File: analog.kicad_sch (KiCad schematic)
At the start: 47 parts, among them J10 Sensor harness, U8 ADS1115

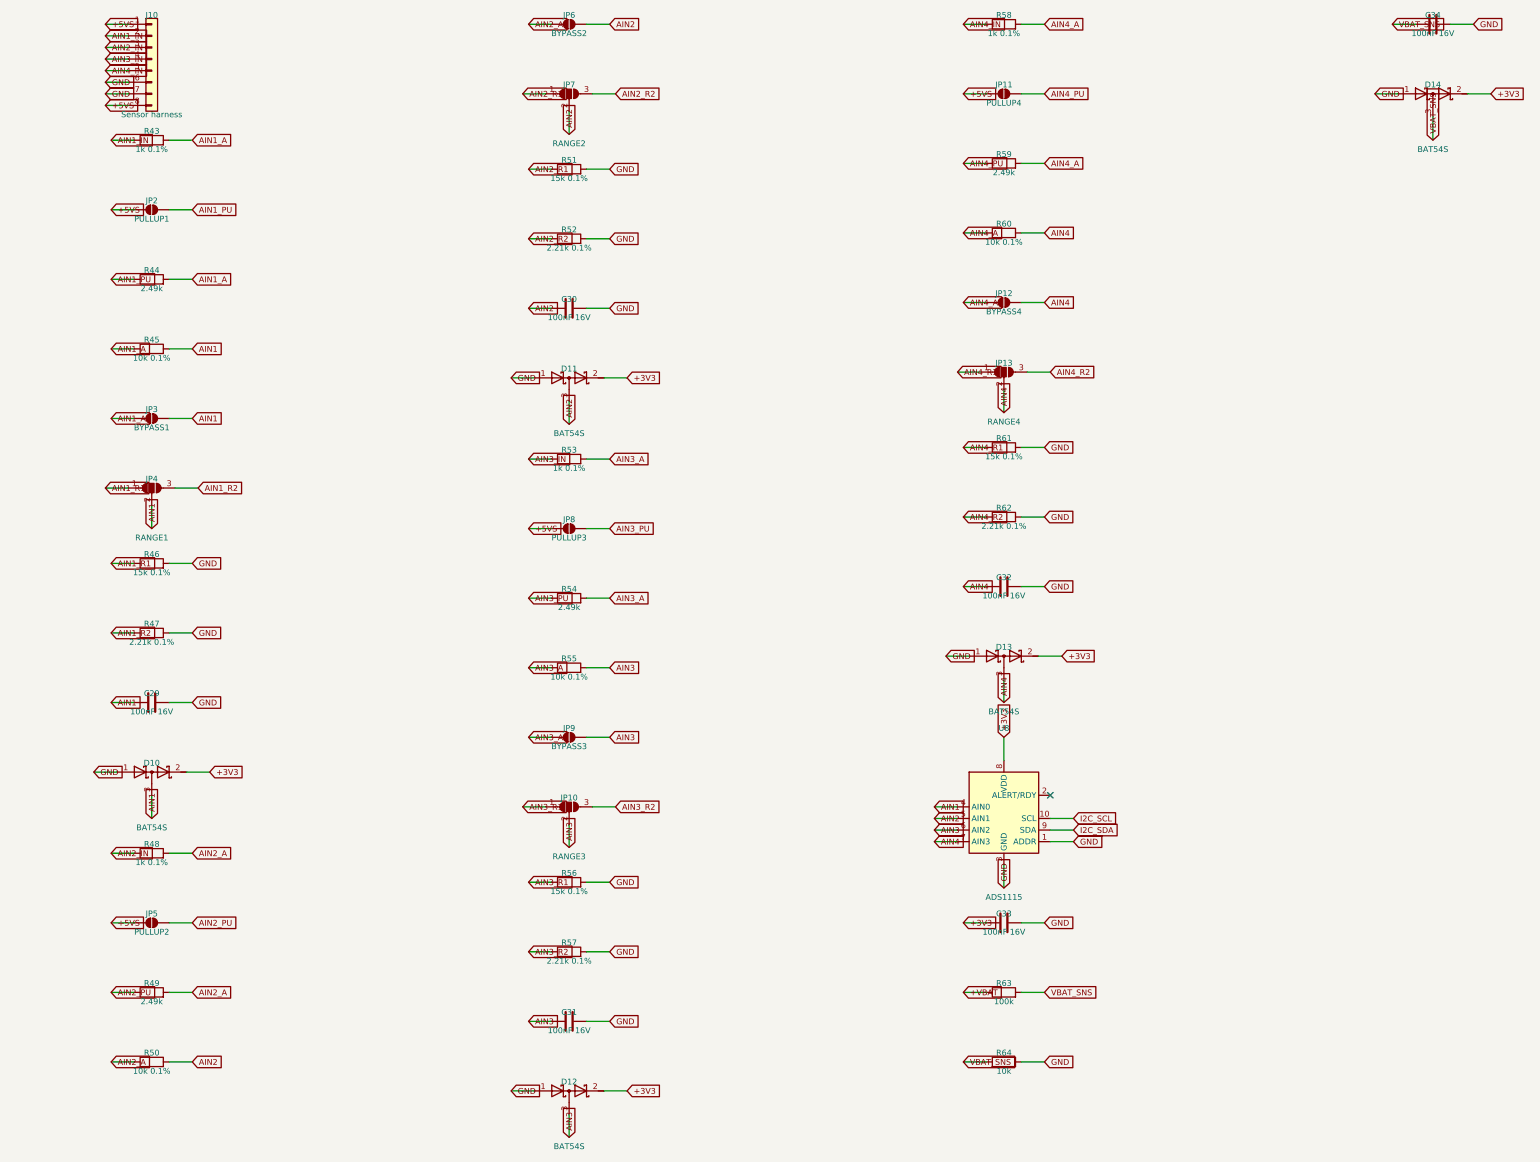
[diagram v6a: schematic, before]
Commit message: Schematic: power symbols and readable text placement (items 1-2 of 5)
The schematic was a netlist drawn as a picture: 486 global labels for 108
nets, roughly four per net, every part an island with a name flag on each
pin and no wires between anything. You could not trace a circuit by eye.
That is a fair description of a document that fails at the one thing a
schematic is for, and it is on me -- the generator was built to produce a
correct netlist and the drawing was an afterthought.

Two of the five agreed fixes are in:

Rails are power symbols. GND, +3V3, +5V, +5VS, +VBAT, VBUS and SD_VDD now
carry a proper power symbol instead of a net-name label -- 190 of them,
taking the label count from 486 to 296. Where KiCad has no stock symbol
for a rail a generic one is instantiated with its Value overridden, which
is how KiCad names a power net; validate.py re-extracts through KiCad and
compares node-for-node, so a wrong guess there would fail the build rather
than quietly merge two rails. PWR_FLAG keeps a label: pairing it with a
power symbol makes an island of two symbols that declares a rail and
connects to nothing visible.

Text no longer collides. Labels were all justified left, so any label
pointing back at its own component ran its text over the body -- RON_5V
across R4, SW_5V across L1; they now justify away from the part.
Reference and value sat hard against the symbol, so a pin leaving the top
or bottom put its stub and power symbol straight through them: "LM5164
(5V)" printed through the GND symbol under U2. Both now clear the stub,
and the row height accounts for it so the clearance does not just push
the collision into the next row. Power symbol references are hidden, as
they are in every schematic.

Also fixed: the packer wrapped on height but never on width, so the power
sheet silently ran off the 420 mm page -- two symbols landed at x = 422.9
where ERC reported them unconnected and nothing else complained. It now
fails loudly.

Items 3-5 (real hierarchy, w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
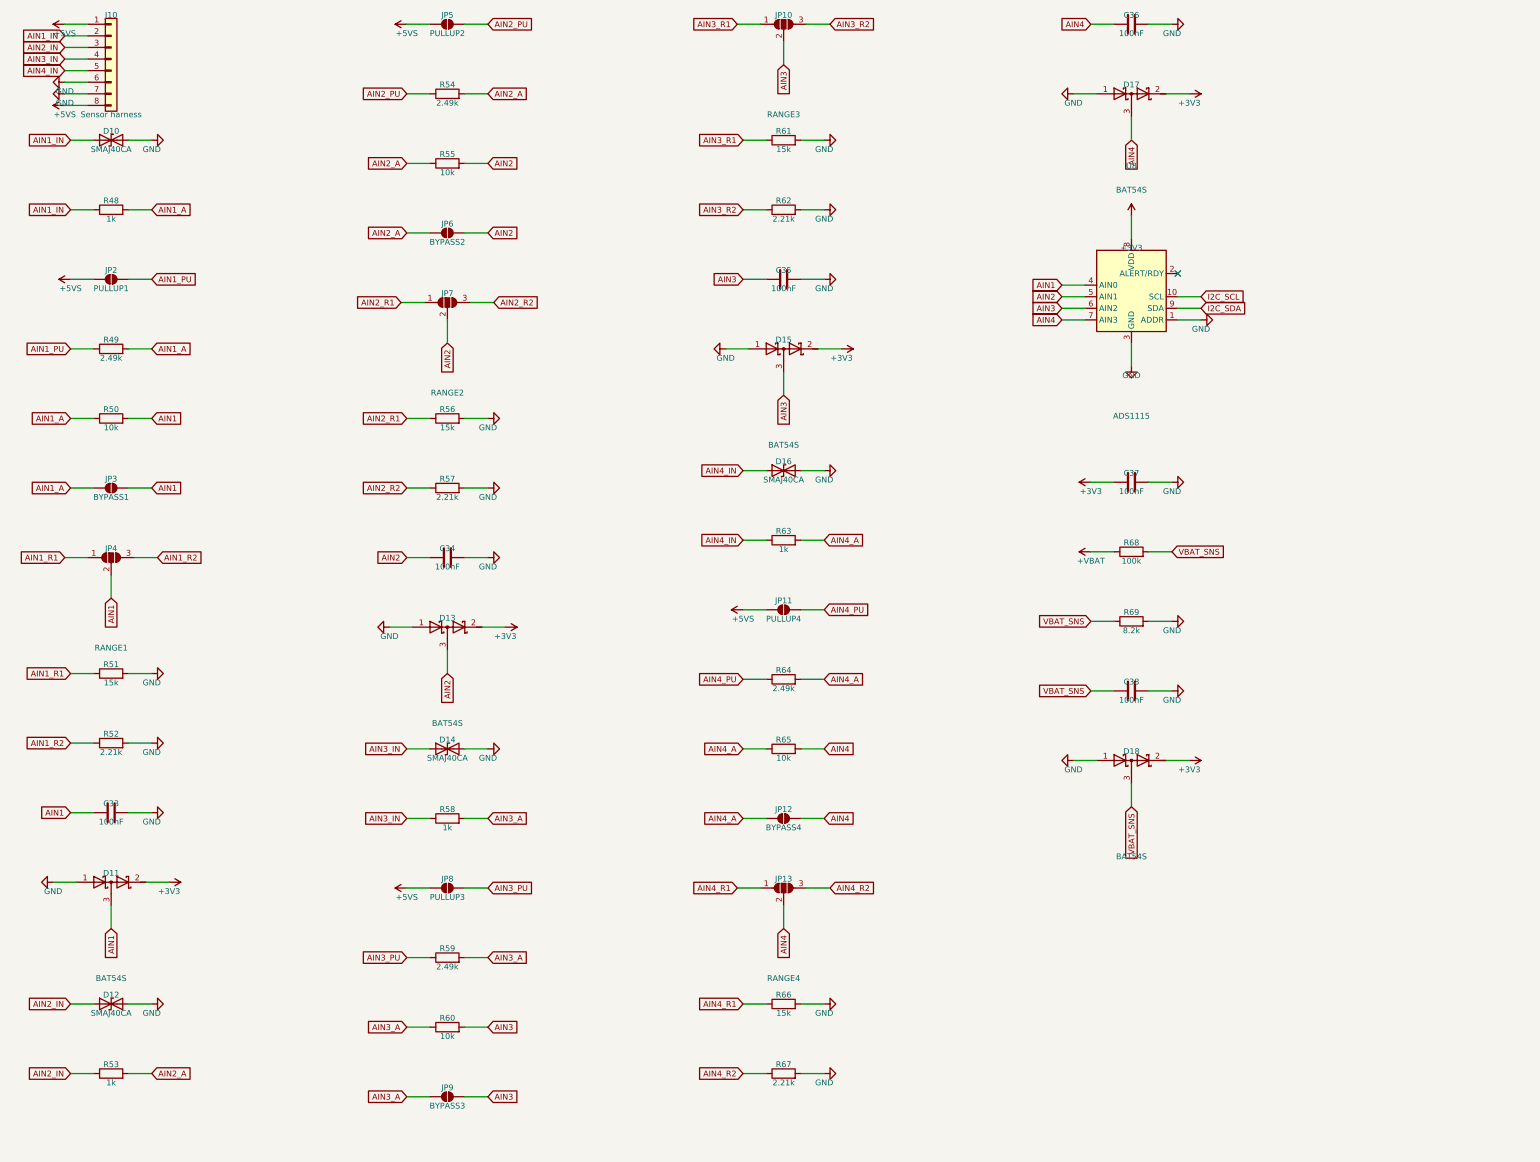
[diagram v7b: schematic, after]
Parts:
- removed C29, C30, C31, C32: 100nF 16V, Capacitor_SMD:C_0805_2012Metric, symbol Device:C
- removed R43: 1k 0.1%, Resistor_SMD:R_0805_2012Metric, symbol Device:R
- removed R44: 2.49k, Resistor_SMD:R_0805_2012Metric, symbol Device:R
- removed R45: 10k 0.1%, Resistor_SMD:R_0805_2012Metric, symbol Device:R
- removed R46: 15k 0.1%, Resistor_SMD:R_0805_2012Metric, symbol Device:R
- removed R47: 2.21k 0.1%, Resistor_SMD:R_0805_2012Metric, symbol Device:R
- added C35, C36, C37, C38: 100nF, Capacitor_SMD:C_0805_2012Metric, symbol Device:C
- added D15, D17, D18: BAT54S, Package_TO_SOT_SMD:SOT-23, symbol Device:D_Schottky_Dual_Series_AKC
- added D16: SMAJ40CA, Diode_SMD:D_SMA, symbol Device:D_TVS
- added R65: 10k, Resistor_SMD:R_0805_2012Metric, symbol Device:R
- added R66: 15k, Resistor_SMD:R_0805_2012Metric, symbol Device:R
- added R67: 2.21k, Resistor_SMD:R_0805_2012Metric, symbol Device:R
- added R68: 100k, Resistor_SMD:R_0805_2012Metric, symbol Device:R
- added R69: 8.2k, Resistor_SMD:R_0805_2012Metric, symbol Device:R
- C33: value 100nF 16V -> 100nF; Note ADS1115 decoupling -> Ch1 anti-alias / ADC charge reservoir; Voltage (none) -> 16V
- C34: value 100nF 16V -> 100nF; Note (none) -> Ch2 anti-alias / ADC charge reservoir; Voltage (none) -> 16V
- D10: value BAT54S -> SMAJ40CA; footprint Package_TO_SOT_SMD:SOT-23 -> Diode_SMD:D_SMA; symbol Device:D_Schottky_Dual_Series_AKC -> Device:D_TVS; MPN BAT54S -> Littelfuse SMAJ40CA; Note Ch1 rail clamp (both polarities) -> Ch1 harness transient clamp (bidirectional, 400W)
- D11: Note Ch2 rail clamp (both polarities) -> Ch1 rail clamp (both polarities)
- D12: value BAT54S -> SMAJ40CA; footprint Package_TO_SOT_SMD:SOT-23 -> Diode_SMD:D_SMA; symbol Device:D_Schottky_Dual_Series_AKC -> Device:D_TVS; MPN BAT54S -> Littelfuse SMAJ40CA; Note Ch3 rail clamp (both polarities) -> Ch2 harness transient clamp (bidirectional, 400W)
- D13: Note Ch4 rail clamp (both polarities) -> Ch2 rail clamp (both polarities)
- D14: value BAT54S -> SMAJ40CA; footprint Package_TO_SOT_SMD:SOT-23 -> Diode_SMD:D_SMA; symbol Device:D_Schottky_Dual_Series_AKC -> Device:D_TVS; MPN BAT54S -> Littelfuse SMAJ40CA; Note Battery-monitor clamp -> Ch3 harness transient clamp (bidirectional, 400W)
- R48: value 1k 0.1% -> 1k; Note Ch2 series/fault-current limit; 0.1% thin film -- it is ins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 -> Ch1 series/fault-current limit; 0.1% thin film -- it is ins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; Tolerance (none) -> 0.1%
- R49: Note Ch2 bias resistor -> Ch1 bias resistor
- R50: value 10k 0.1% -> 10k; Note Ch2 divider upper leg, 0.1% thin film for AFR-grade accuracy -> Ch1 divider upper leg, 0.1% thin film for AFR-grade accuracy; Tolerance (none) -> 0.1%
- R51, R56, R61: value 15k 0.1% -> 15k; Tolerance (none) -> 0.1%
- R52, R57, R62: value 2.21k 0.1% -> 2.21k; Tolerance (none) -> 0.1%
- R53: value 1k 0.1% -> 1k; Note Ch3 series/fault-current limit; 0.1% thin film -- it is ins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 -> Ch2 series/fault-current limit; 0.1% thin film -- it is ins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; Tolerance (none) -> 0.1%
- R54: Note Ch3 bias resistor -> Ch2 bias resistor
- R55: value 10k 0.1% -> 10k; Note Ch3 divider upper leg, 0.1% thin film for AFR-grade accuracy -> Ch2 divider upper leg, 0.1% thin film for AFR-grade accuracy; Tolerance (none) -> 0.1%
- R58: value 1k 0.1% -> 1k; Note Ch4 series/fault-current limit; 0.1% thin film -- it is ins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 -> Ch3 series/fault-current limit; 0.1% thin film -- it is ins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; Tolerance (none) -> 0.1%
- R59: Note Ch4 bias resistor -> Ch3 bias resistor
- R60: value 10k 0.1% -> 10k; Note Ch4 divider upper leg, 0.1% thin film for AFR-grade accuracy -> Ch3 divider upper leg, 0.1% thin film for AFR-grade accuracy; Tolerance (none) -> 0.1%
- R63: value 100k -> 1k; Note Battery monitor: divide by 11 -> Ch4 series/fault-current limit; 0.1% thin film -- it is ins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; Tolerance (none) -> 0.1%
- R64: value 10k -> 2.49k; Note (none) -> Ch4 bias resistor
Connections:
- net +3V3: now also C37.1, D15.2 (K), D17.2 (K), D18.2 (K); no longer C33.1, D10.2 (K), D12.2 (K), D14.2 (K)
- net +VBAT: now also R68.1; no longer R63.1
- net AIN1: now also C33.1, D11.3 (common), R50.2; no longer D10.3 (common)
- net AIN1_A: now also R48.2, R49.2, R50.1
- net AIN1_IN: now also D10.1 (A1), R48.1
- net AIN1_PU: now also R49.1
- net AIN1_R1: now also R51.1
- net AIN1_R2: now also R52.1
- net AIN2: now also C34.1, D13.3 (common), R55.2; no longer D11.3 (common), R50.2
- net AIN2_A: now also R53.2, R54.2, R55.1; no longer R48.2, R49.2, R50.1
- net AIN2_IN: now also D12.1 (A1), R53.1; no longer R48.1
- net AIN2_PU: now also R54.1; no longer R49.1
- net AIN2_R1: now also R56.1; no longer R51.1
- net AIN2_R2: now also R57.1; no longer R52.1
- net AIN3: now also R60.2, C35.1, D15.3 (common); no longer D12.3 (common), R55.2
- net AIN3_A: now also R58.2, R59.2, R60.1; no longer R53.2, R54.2, R55.1
- net AIN3_IN: now also D14.1 (A1), R58.1; no longer R53.1
- net AIN3_PU: now also R59.1; no longer R54.1
- net AIN3_R1: now also R61.1; no longer R56.1
- net AIN3_R2: now also R62.1; no longer R57.1
- net AIN4: now also C36.1, D17.3 (common), R65.2; no longer D13.3 (common), R60.2
- net AIN4_A: now also R63.2, R64.2, R65.1; no longer R58.2, R59.2, R60.1
- net AIN4_IN: now also R63.1, D16.1 (A1); no longer R58.1
- net AIN4_PU: now also R64.1; no longer R59.1
- net AIN4_R1: now also R66.1; no longer R61.1
- net AIN4_R2: now also R67.1; no longer R62.1
- net GND: now also D10.2 (A2), D12.2 (A2), D14.2 (A2), C35.2, C36.2, C37.2, C38.2, D15.1 (A), D16.2 (A2), D17.1 (A), D18.1 (A), R66.2, R67.2, R69.2; no longer D10.1 (A), D12.1 (A), D14.1 (A), R64.2
- net VBAT_SNS: now also C38.1, D18.3 (common), R68.2, R69.1; no longer C34.1, D14.3 (common), R63.2, R64.1
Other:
- moved on the sheet: C33, C34, D11, D13, J10, JP10, JP11, JP12, JP13, JP2, JP3, JP4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
